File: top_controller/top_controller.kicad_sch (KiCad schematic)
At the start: 117 parts, among them J1 OUT1, J10 USB_C_Receptacle_USB2.0, J11 SWD, J12 UART, J13 BOOT0, J14 BOOT1, J2 OUT2, J3 OUT3, J4 OUT4, J5 OUT5, J6 OUT6, J7 OUT7, J8 OUT8, J9 PIN, SW1 RESET, U1 STM32F103C8Tx, U2 LT3045xMSE, U3 AD5754BREZ, U4 AD5754BREZ, U5 REF192, U6 EPM78V2, U7 REF192, Y1 8MHz

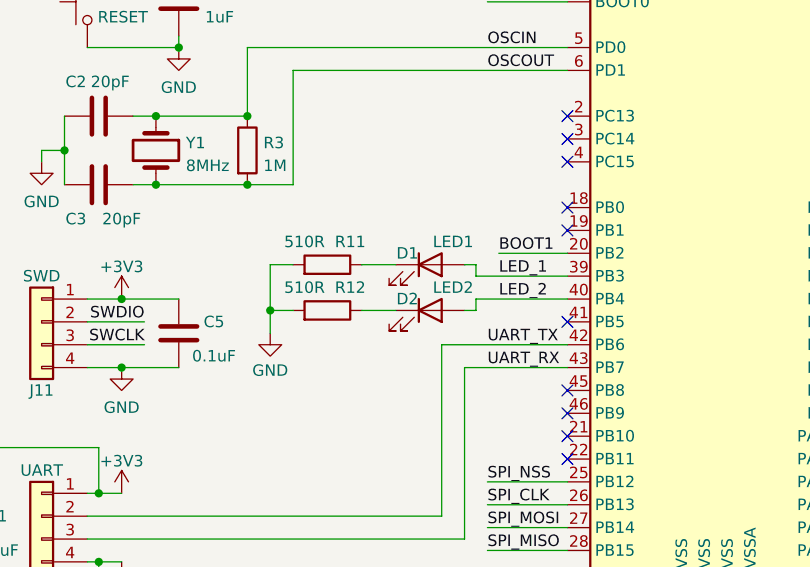
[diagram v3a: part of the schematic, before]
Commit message: Changed STM LED pins to more convenient ones
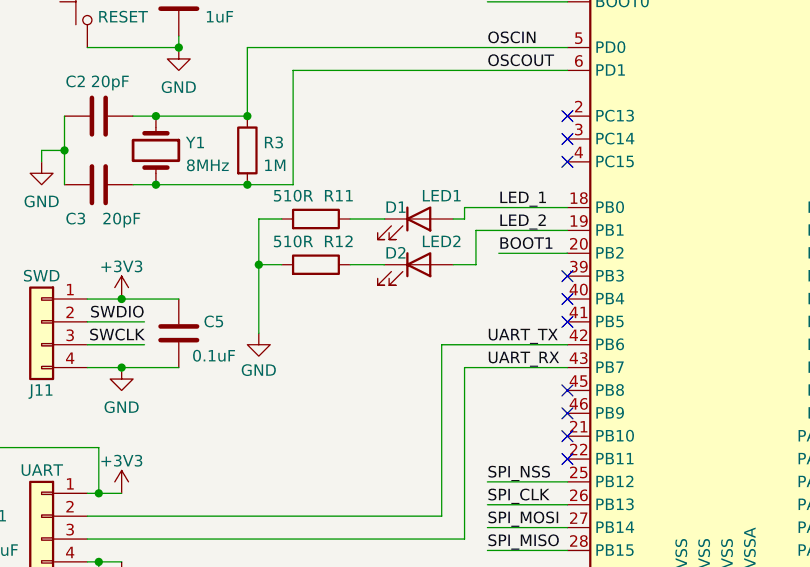
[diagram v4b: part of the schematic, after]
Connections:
- net LED_1: now also U1.18 (PB0); no longer U1.39 (PB3)
- net LED_2: now also U1.19 (PB1); no longer U1.40 (PB4)
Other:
- moved on the sheet: D1, D2, R11, R12
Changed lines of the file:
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@@
   (junction (at 87.63 194.31) (diameter 0) (color 0 0 0 0)
   )
+  (junction (at 49.53 71.12) (diameter 0) (color 0 0 0 0)
+  )
   (junction (at 154.94 146.05) (diameter 0) (color 0 0 0 0)
   )
@@
   (junction (at 212.09 64.77) (diameter 0) (color 0 0 0 0)
   )
-  (junction (at 50.8 76.2) (diameter 0) (color 0 0 0 0)
-  )
   (junction (at 223.52 148.59) (diameter 0) (color 0 0 0 0)
   )
@@
   (junction (at 226.06 90.17) (diameter 0) (color 0 0 0 0)
   )
-  (no_connect (at 83.82 64.77))
+  (no_connect (at 83.82 72.39))
   (no_connect (at 83.82 59.69))
   (no_connect (at 83.82 77.47))
@@
   (no_connect (at 83.82 90.17))
   (no_connect (at 199.39 45.72))
+  (no_connect (at 83.82 74.93))
   (no_connect (at 83.82 54.61))
   (no_connect (at 83.82 57.15))
   (no_connect (at 116.84 90.17))
   (no_connect (at 273.05 53.34))
-  (no_connect (at 83.82 67.31))
   (no_connect (at 199.39 53.34))
   (no_connect (at 83.82 92.71))
@@
     (stroke (width 0) (type default))
   )
+  (wire (pts (xy 72.39 64.77) (xy 83.82 64.77))
+    (stroke (width 0) (type default))
+  )
   (wire (pts (xy 189.23 148.59) (xy 189.23 147.32))
     (stroke (width 0) (type default))
@@
     (stroke (width 0) (type default))
   )
-  (wire (pts (xy 73.66 72.39) (xy 83.82 72.39))
-    (stroke (width 0) (type default))
-  )
   (wire (pts (xy 223.52 143.51) (xy 223.52 148.59))
     (stroke (width 0) (type default))
@@
     (stroke (width 0) (type default))
   )
-  (wire (pts (xy 73.66 76.2) (xy 73.66 74.93))
-    (stroke (width 0) (type default))
-  )
   (wire (pts (xy 194.31 147.32) (xy 189.23 147.32))
     (stroke (width 0) (type default))
@@
     (stroke (width 0) (type default))
   )
-  (wire (pts (xy 73.66 71.12) (xy 73.66 72.39))
-    (stroke (width 0) (type default))
-  )
   (wire (pts (xy 219.71 64.77) (xy 227.33 64.77))
     (stroke (width 0) (type default))
@@
     (stroke (width 0) (type default))
   )
-  (wire (pts (xy 238.76 148.59) (xy 252.73 148.59))
+  (wire (pts (xy 49.53 71.12) (xy 49.53 78.74))
     (stroke (width 0) (type default))
   )
-  (wire (pts (xy 144.78 167.64) (xy 144.78 181.61))
+  (wire (pts (xy 238.76 148.59) (xy 252.73 148.59))
     (stroke (width 0) (type default))
   )
-  (wire (pts (xy 50.8 71.12) (xy 50.8 76.2))
+  (wire (pts (xy 144.78 167.64) (xy 144.78 181.61))
     (stroke (width 0) (type default))
   )
@@
     (stroke (width 0) (type default))
   )
-  (wire (pts (xy 64.77 76.2) (xy 60.96 76.2))
+  (wire (pts (xy 63.5 71.12) (xy 59.69 71.12))
     (stroke (width 0) (type default))
   )
@@
     (stroke (width 0) (type default))
   )
+  (wire (pts (xy 73.66 67.31) (xy 73.66 71.12))
+    (stroke (width 0) (type default))
+  )
   (wire (pts (xy 252.73 148.59) (xy 266.7 148.59))
     (stroke (width 0) (type default))
@@
     (stroke (width 0) (type default))
   )
-  (wire (pts (xy 53.34 71.12) (xy 50.8 71.12))
+  (wire (pts (xy 52.07 66.04) (xy 49.53 66.04))
     (stroke (width 0) (type default))
   )
@@
     (stroke (width 0) (type default))
   )
+  (wire (pts (xy 83.82 67.31) (xy 73.66 67.31))
+    (stroke (width 0) (type default))
+  )
   (wire (pts (xy 139.7 49.53) (xy 147.32 49.53))
     (stroke (width 0) (type default))
@@
     (stroke (width 0) (type default))
   )
-  (wire (pts (xy 50.8 76.2) (xy 50.8 78.74))
+  (wire (pts (xy 49.53 66.04) (xy 49.53 71.12))
     (stroke (width 0) (type default))
   )
@@
     (stroke (width 0) (type default))
   )
+  (wire (pts (xy 72.39 66.04) (xy 72.39 64.77))
+    (stroke (width 0) (type default))
+  )
   (wire (pts (xy 132.08 29.21) (xy 132.08 25.4))
     (stroke (width 0) (type default))
@@
     (stroke (width 0) (type default))
   )
-  (wire (pts (xy 53.34 76.2) (xy 50.8 76.2))
+  (wire (pts (xy 49.53 71.12) (xy 52.07 71.12))
     (stroke (width 0) (type default))
   )
@@
     (stroke (width 0) (type default))
   )
-  (wire (pts (xy 73.66 74.93) (xy 83.82 74.93))
-    (stroke (width 0) (type default))
-  )
   (wire (pts (xy 97.79 194.31) (xy 111.76 194.31))
     (stroke (width 0) (type default))
@@
     (stroke (width 0) (type default))
   )
-  (wire (pts (xy 72.39 76.2) (xy 73.66 76.2))
+  (wire (pts (xy 71.12 71.12) (xy 73.66 71.12))
     (stroke (width 0) (type default))
   )
@@
     (stroke (width 0) (type default))
   )
-  (wire (pts (xy 64.77 71.12) (xy 60.96 71.12))
+  (wire (pts (xy 63.5 66.04) (xy 59.69 66.04))
     (stroke (width 0) (type default))
   )
@@
     (stroke (width 0) (type default))
   )
-  (wire (pts (xy 72.39 71.12) (xy 73.66 71.12))
+  (wire (pts (xy 71.12 66.04) (xy 72.39 66.04))
     (stroke (width 0) (type default))
   )
@@
     (effects (font (size 1.27 1.27)) (justify right bottom))
   )
-  (label "LED_1" (at 76.2 72.39 0) (fields_autoplaced)
+  (label "LED_1" (at 76.2 64.77 0) (fields_autoplaced)
     (effects (font (size 1.27 1.27)) (justify left bottom))
   )
@@
     (effects (font (size 1.27 1.27)) (justify right bottom))
   )
-  (label "LED_2" (at 76.2 74.93 0) (fields_autoplaced)
+  (label "LED_2" (at 76.2 67.31 0) (fields_autoplaced)
     (effects (font (size 1.27 1.27)) (justify left bottom))
   )
@@
     )
   )
-  (symbol (lib_id "Device:LED") (at 68.58 76.2 0) (unit 1)
+  (symbol (lib_id "Device:LED") (at 67.31 71.12 0) (unit 1)
     (in_bom yes) (on_board yes) (dnp no)
-    (property "Reference" "D2" (at 66.04 74.93 0)
+    (property "Reference" "D2" (at 64.77 69.85 0)
       (effects (font (size 1.27 1.27)))
     )
-    (property "Value" "LED2" (at 71.12 73.66 0)
+    (property "Value" "LED2" (at 69.85 68.58 0)
       (effects (font (size 1.27 1.27)))
     )
-    (property "Footprint" "LED_SMD:LED_0805_2012Metric" (at 68.58 76.2 0)
+    (property "Footprint" "LED_SMD:LED_0805_2012Metric" (at 67.31 71.12 0)
       (effects (font (size 1.27 1.27)) hide)
     )
-    (property "Datasheet" "~" (at 68.58 76.2 0)
+    (property "Datasheet" "~" (at 67.31 71.12 0)
       (effects (font (size 1.27 1.27)) hide)
     )
@@
     )
   )
-  (symbol (lib_id "Device:R") (at 57.15 71.12 270) (mirror x) (unit 1)
+  (symbol (lib_id "Device:R") (at 55.88 66.04 270) (mirror x) (unit 1)
     (in_bom yes) (on_board yes) (dnp no)
-    (property "Reference" "R11" (at 59.69 68.58 90)
+    (property "Reference" "R11" (at 58.42 63.5 90)
       (effects (font (size 1.27 1.27)))
     )
-    (property "Value" "510R" (at 54.61 68.58 90)
+    (property "Value" "510R" (at 53.34 63.5 90)
       (effects (font (size 1.27 1.27)))
     )
-    (property "Footprint" "Resistor_SMD:R_0603_1608Metric" (at 57.15 72.898 90)
+    (property "Footprint" "Resistor_SMD:R_0603_1608Metric" (at 55.88 67.818 90)
       (effects (font (size 1.27 1.27)) hide)
     )
-    (property "Datasheet" "~" (at 57.15 71.12 0)
+    (property "Datasheet" "~" (at 55.88 66.04 0)
       (effects (font (size 1.27 1.27)) hide)
     )
@@
     )
   )
-  (symbol (lib_id "power:GND") (at 50.8 78.74 0) (unit 1)
+  (symbol (lib_id "power:GND") (at 49.53 78.74 0) (unit 1)
     (in_bom yes) (on_board yes) (dnp no) (fields_autoplaced)
-    (property "Reference" "#PWR016" (at 50.8 85.09 0)
+    (property "Reference" "#PWR016" (at 49.53 85.09 0)
       (effects (font (size 1.27 1.27)) hide)
     )
-    (property "Value" "GND" (at 50.8 82.8755 0)
+    (property "Value" "GND" (at 49.53 82.8755 0)
       (effects (font (size 1.27 1.27)))
     )
-    (property "Footprint" "" (at 50.8 78.74 0)
+    (property "Footprint" "" (at 49.53 78.74 0)
       (effects (font (size 1.27 1.27)) hide)
     )
-    (property "Datasheet" "" (at 50.8 78.74 0)
+    (property "Datasheet" "" (at 49.53 78.74 0)
       (effects (font (size 1.27 1.27)) hide)
     )
@@
     )
   )
-  (symbol (lib_id "Device:R") (at 57.15 76.2 270) (mirror x) (unit 1)
+  (symbol (lib_id "Device:R") (at 55.88 71.12 270) (mirror x) (unit 1)
     (in_bom yes) (on_board yes) (dnp no)
-    (property "Reference" "R12" (at 59.69 73.66 90)
+    (property "Reference" "R12" (at 58.42 68.58 90)
       (effects (font (size 1.27 1.27)))
     )
-    (property "Value" "510R" (at 54.61 73.66 90)
+    (property "Value" "510R" (at 53.34 68.58 90)
       (effects (font (size 1.27 1.27)))
     )
-    (property "Footprint" "Resistor_SMD:R_0603_1608Metric" (at 57.15 77.978 90)
+    (property "Footprint" "Resistor_SMD:R_0603_1608Metric" (at 55.88 72.898 90)
       (effects (font (size 1.27 1.27)) hide)
     )
-    (property "Datasheet" "~" (at 57.15 76.2 0)
+    (property "Datasheet" "~" (at 55.88 71.12 0)
       (effects (font (size 1.27 1.27)) hide)
     )
@@
     )
   )
-  (symbol (lib_id "Device:LED") (at 68.58 71.12 0) (unit 1)
+  (symbol (lib_id "Device:LED") (at 67.31 66.04 0) (unit 1)
     (in_bom yes) (on_board yes) (dnp no)
-    (property "Reference" "D1" (at 66.04 69.85 0)
+    (property "Reference" "D1" (at 64.77 64.77 0)
       (effects (font (size 1.27 1.27)))
     )
-    (property "Value" "LED1" (at 71.12 68.58 0)
+    (property "Value" "LED1" (at 69.85 63.5 0)
       (effects (font (size 1.27 1.27)))
     )
-    (property "Footprint" "LED_SMD:LED_0805_2012Metric" (at 68.58 71.12 0)
+    (property "Footprint" "LED_SMD:LED_0805_2012Metric" (at 67.31 66.04 0)
       (effects (font (size 1.27 1.27)) hide)
     )
-    (property "Datasheet" "~" (at 68.58 71.12 0)
+    (property "Datasheet" "~" (at 67.31 66.04 0)
       (effects (font (size 1.27 1.27)) hide)
     )

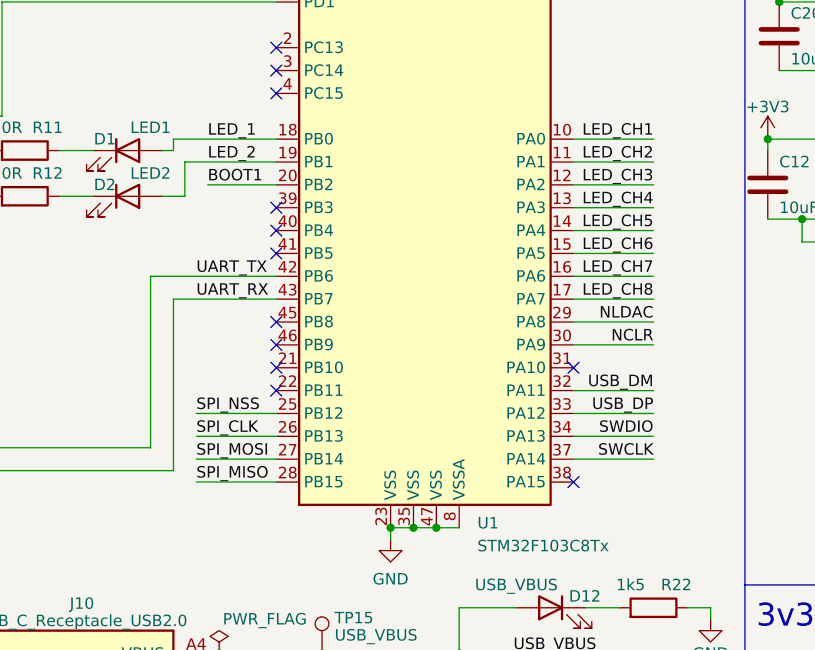
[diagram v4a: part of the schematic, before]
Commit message: Changed data pins on STM32 for easier tracing
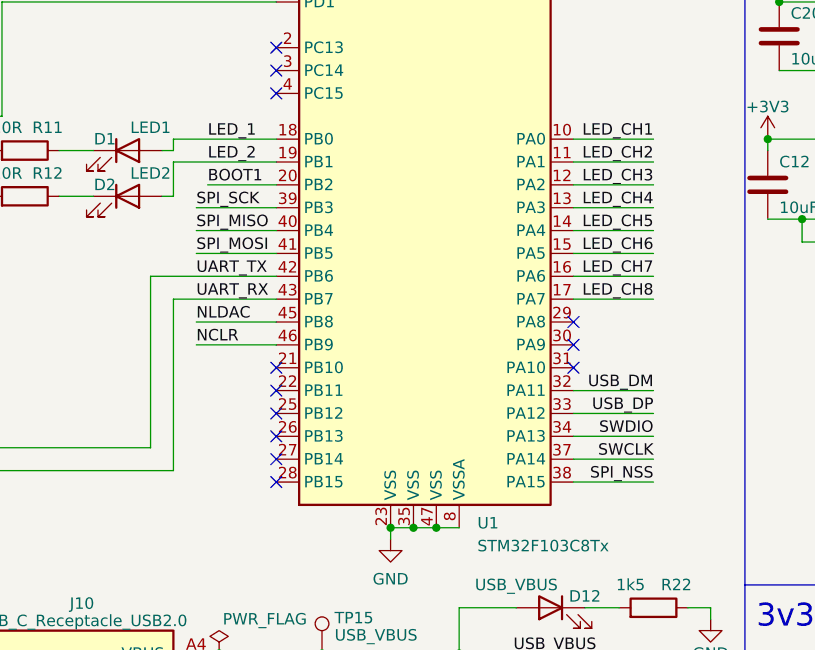
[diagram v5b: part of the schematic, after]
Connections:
- net NCLR: now also U1.46 (PB9); no longer U1.30 (PA9)
- net NLDAC: now also U1.45 (PB8); no longer U1.29 (PA8)
- net SPI_CLK: no longer U1.26 (PB13)
- net SPI_MISO: now also U1.40 (PB4); no longer U1.28 (PB15)
- net SPI_MOSI: now also U1.41 (PB5); no longer U1.27 (PB14)
- net SPI_NSS: now also U1.38 (PA15); no longer U1.25 (PB12)
- net SPI_SCK: now reaches U1.39 (PB3)
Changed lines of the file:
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@@
   (junction (at 226.06 90.17) (diameter 0) (color 0 0 0 0)
   )
-  (no_connect (at 83.82 72.39))
   (no_connect (at 83.82 59.69))
-  (no_connect (at 83.82 77.47))
+  (no_connect (at 83.82 95.25))
   (no_connect (at 273.05 48.26))
+  (no_connect (at 116.84 87.63))
   (no_connect (at 83.82 90.17))
   (no_connect (at 199.39 45.72))
-  (no_connect (at 83.82 74.93))
+  (no_connect (at 83.82 100.33))
   (no_connect (at 83.82 54.61))
   (no_connect (at 83.82 57.15))
@@
   (no_connect (at 273.05 53.34))
   (no_connect (at 199.39 53.34))
+  (no_connect (at 116.84 85.09))
   (no_connect (at 83.82 92.71))
+  (no_connect (at 83.82 97.79))
   (no_connect (at 273.05 45.72))
   (no_connect (at 273.05 50.8))
-  (no_connect (at 83.82 85.09))
-  (no_connect (at 116.84 102.87))
-  (no_connect (at 83.82 87.63))
+  (no_connect (at 83.82 102.87))
   (no_connect (at 199.39 50.8))
   (no_connect (at 199.39 48.26))
@@
     (stroke (width 0) (type default))
   )
-  (wire (pts (xy 74.93 102.87) (xy 83.82 102.87))
-    (stroke (width 0) (type default))
-  )
   (wire (pts (xy 116.84 170.18) (xy 116.84 176.53))
     (stroke (width 0) (type default))
@@
     (stroke (width 0) (type default))
   )
+  (wire (pts (xy 74.93 85.09) (xy 83.82 85.09))
+    (stroke (width 0) (type default))
+  )
   (wire (pts (xy 148.59 137.16) (xy 152.4 137.16))
     (stroke (width 0) (type default))
@@
     (stroke (width 0) (type default))
   )
-  (polyline (pts (xy 127 86.36) (xy 127 86.36))
-    (stroke (width 0) (type default))
-  )
   (wire (pts (xy 238.76 147.32) (xy 238.76 148.59))
     (stroke (width 0) (type default))
@@
     (stroke (width 0) (type default))
   )
-  (wire (pts (xy 73.66 67.31) (xy 73.66 71.12))
+  (wire (pts (xy 72.39 67.31) (xy 72.39 71.12))
     (stroke (width 0) (type default))
   )
@@
     (stroke (width 0) (type default))
   )
+  (wire (pts (xy 74.93 72.39) (xy 83.82 72.39))
+    (stroke (width 0) (type default))
+  )
   (wire (pts (xy 116.84 77.47) (xy 125.73 77.47))
     (stroke (width 0) (type default))
@@
     (stroke (width 0) (type default))
   )
-  (wire (pts (xy 83.82 67.31) (xy 73.66 67.31))
+  (wire (pts (xy 83.82 67.31) (xy 72.39 67.31))
     (stroke (width 0) (type default))
   )
@@
     (stroke (width 0) (type default))
   )
+  (wire (pts (xy 74.93 74.93) (xy 83.82 74.93))
+    (stroke (width 0) (type default))
+  )
   (wire (pts (xy 104.14 116.84) (xy 104.14 121.92))
     (stroke (width 0) (type default))
@@
     (stroke (width 0) (type default))
   )
+  (wire (pts (xy 74.93 77.47) (xy 83.82 77.47))
+    (stroke (width 0) (type default))
+  )
   (wire (pts (xy 97.79 182.88) (xy 97.79 186.69))
     (stroke (width 0) (type default))
@@
     (stroke (width 0) (type default))
   )
-  (wire (pts (xy 74.93 97.79) (xy 83.82 97.79))
-    (stroke (width 0) (type default))
-  )
   (wire (pts (xy 189.23 128.27) (xy 189.23 129.54))
     (stroke (width 0) (type default))
@@
     (stroke (width 0) (type default))
   )
+  (wire (pts (xy 74.93 87.63) (xy 83.82 87.63))
+    (stroke (width 0) (type default))
+  )
   (wire (pts (xy 46.99 194.31) (xy 57.15 194.31))
     (stroke (width 0) (type default))
@@
     (stroke (width 0) (type default))
   )
-  (wire (pts (xy 116.84 85.09) (xy 125.73 85.09))
-    (stroke (width 0) (type default))
-  )
   (wire (pts (xy 148.59 129.54) (xy 154.94 129.54))
     (stroke (width 0) (type default))
@@
     (stroke (width 0) (type default))
   )
+  (wire (pts (xy 116.84 102.87) (xy 125.73 102.87))
+    (stroke (width 0) (type default))
+  )
   (wire (pts (xy 30.48 46.99) (xy 40.64 46.99))
     (stroke (width 0) (type default))
@@
     (stroke (width 0) (type default))
   )
-  (wire (pts (xy 71.12 71.12) (xy 73.66 71.12))
+  (wire (pts (xy 71.12 71.12) (xy 72.39 71.12))
     (stroke (width 0) (type default))
   )
@@
     (stroke (width 0) (type default))
   )
-  (wire (pts (xy 74.93 95.25) (xy 83.82 95.25))
-    (stroke (width 0) (type default))
-  )
   (wire (pts (xy 144.78 35.56) (xy 153.67 35.56))
     (stroke (width 0) (type default))
@@
     (stroke (width 0) (type default))
   )
-  (wire (pts (xy 116.84 87.63) (xy 125.73 87.63))
-    (stroke (width 0) (type default))
-  )
   (wire (pts (xy 226.06 106.68) (xy 226.06 102.87))
     (stroke (width 0) (type default))
@@
   )
   (wire (pts (xy 31.75 96.52) (xy 30.48 96.52))
-    (stroke (width 0) (type default))
-  )
-  (wire (pts (xy 74.93 100.33) (xy 83.82 100.33))
     (stroke (width 0) (type default))
   )
@@
     (effects (font (size 1.27 1.27)) (justify left bottom))
   )
-  (label "SPI_CLK" (at 74.93 97.79 0) (fields_autoplaced)
-    (effects (font (size 1.27 1.27)) (justify left bottom))
-  )
   (label "OUT_5" (at 106.68 182.88 270) (fields_autoplaced)
     (effects (font (size 1.27 1.27)) (justify right bottom))
@@
     (effects (font (size 1.27 1.27)) (justify left bottom))
   )
-  (label "SPI_MISO" (at 74.93 102.87 0) (fields_autoplaced)
+  (label "SPI_MOSI" (at 74.93 77.47 0) (fields_autoplaced)
     (effects (font (size 1.27 1.27)) (justify left bottom))
   )
@@
     (effects (font (size 1.27 1.27)) (justify right bottom))
   )
-  (label "SPI_MOSI" (at 74.93 100.33 0) (fields_autoplaced)
-    (effects (font (size 1.27 1.27)) (justify left bottom))
-  )
   (label "USB_VBUS" (at 119.38 121.92 180) (fields_autoplaced)
     (effects (font (size 1.27 1.27)) (justify right bottom))
@@
     (effects (font (size 1.27 1.27)) (justify left bottom))
   )
+  (label "SPI_MISO" (at 74.93 74.93 0) (fields_autoplaced)
+    (effects (font (size 1.27 1.27)) (justify left bottom))
+  )
   (label "USB_VBUS" (at 110.49 151.13 180) (fields_autoplaced)
     (effects (font (size 1.27 1.27)) (justify right bottom))
@@
     (effects (font (size 1.27 1.27)) (justify right bottom))
   )
+  (label "NLDAC" (at 74.93 85.09 0) (fields_autoplaced)
+    (effects (font (size 1.27 1.27)) (justify left bottom))
+  )
   (label "LED_CH1" (at 19.05 175.26 0) (fields_autoplaced)
     (effects (font (size 1.27 1.27)) (justify left bottom))
@@
     (effects (font (size 1.27 1.27)) (justify left bottom))
   )
+  (label "SPI_NSS" (at 125.73 102.87 180) (fields_autoplaced)
+    (effects (font (size 1.27 1.27)) (justify right bottom))
+  )
   (label "SPI_MOSI" (at 144.78 45.72 0) (fields_autoplaced)
     (effects (font (size 1.27 1.27)) (justify left bottom))
@@
   (label "OUT_3" (at 205.74 30.48 180) (fields_autoplaced)
     (effects (font (size 1.27 1.27)) (justify right bottom))
+  )
+  (label "NCLR" (at 74.93 87.63 0) (fields_autoplaced)
+    (effects (font (size 1.27 1.27)) (justify left bottom))
   )
   (label "OSCIN" (at 74.93 46.99 0) (fields_autoplaced)
@@
     (effects (font (size 1.27 1.27)) (justify right bottom))
   )
-  (label "SPI_NSS" (at 74.93 95.25 0) (fields_autoplaced)
-    (effects (font (size 1.27 1.27)) (justify left bottom))
-  )
   (label "NCLR" (at 144.78 38.1 0) (fields_autoplaced)
+    (effects (font (size 1.27 1.27)) (justify left bottom))
+  )
+  (label "SPI_SCK" (at 74.93 72.39 0) (fields_autoplaced)
     (effects (font (size 1.27 1.27)) (justify left bottom))
   )
@@
     (effects (font (face "KiCad Font") (size 1.27 1.27)) (justify right bottom))
   )
-  (label "NLDAC" (at 125.73 85.09 180) (fields_autoplaced)
-    (effects (font (size 1.27 1.27)) (justify right bottom))
-  )
   (label "SWDIO" (at 36.83 77.47 180) (fields_autoplaced)
     (effects (font (size 1.27 1.27)) (justify right bottom))
@@
     (effects (font (size 1.27 1.27)) (justify left bottom))
   )
-  (label "NCLR" (at 125.73 87.63 180) (fields_autoplaced)
-    (effects (font (size 1.27 1.27)) (justify right bottom))
-  )
   (label "NCLR" (at 110.49 142.24 0) (fields_autoplaced)
